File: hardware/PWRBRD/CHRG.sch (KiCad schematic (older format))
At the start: 36 parts

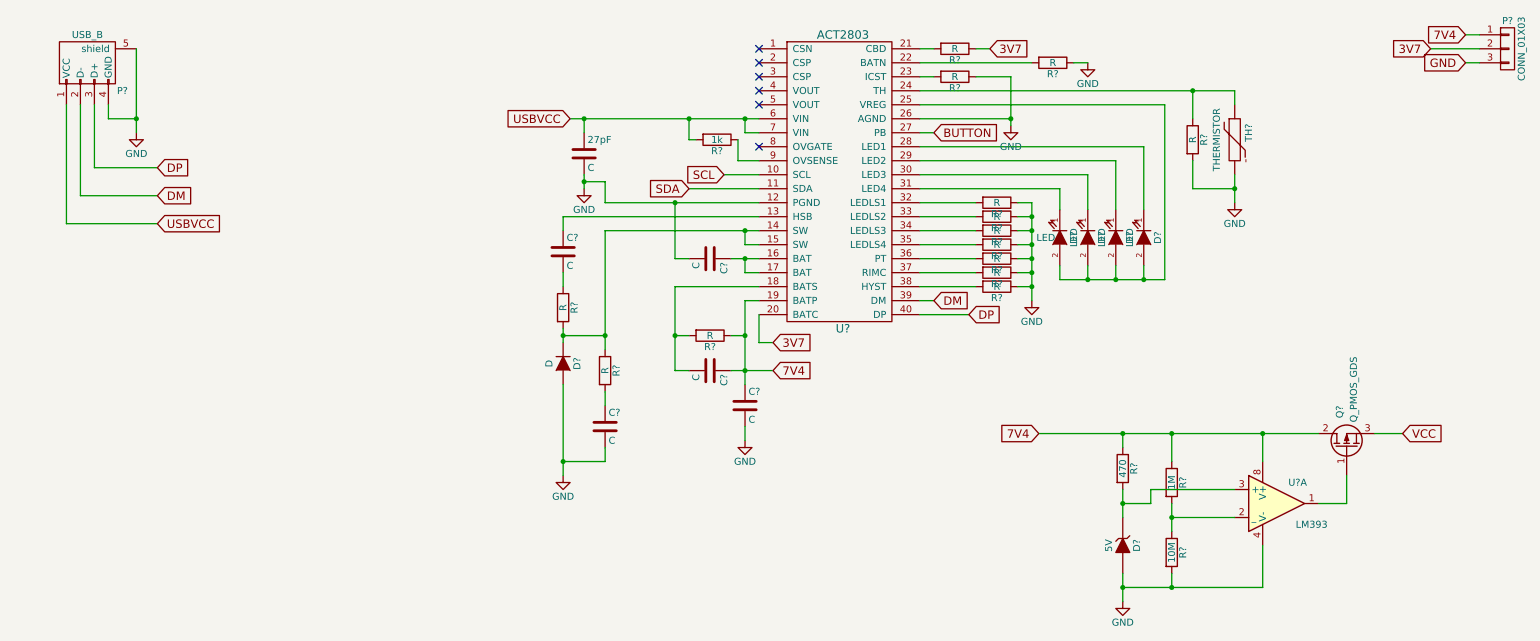
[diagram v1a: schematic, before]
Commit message: Updated the Layout for the BMS portion.
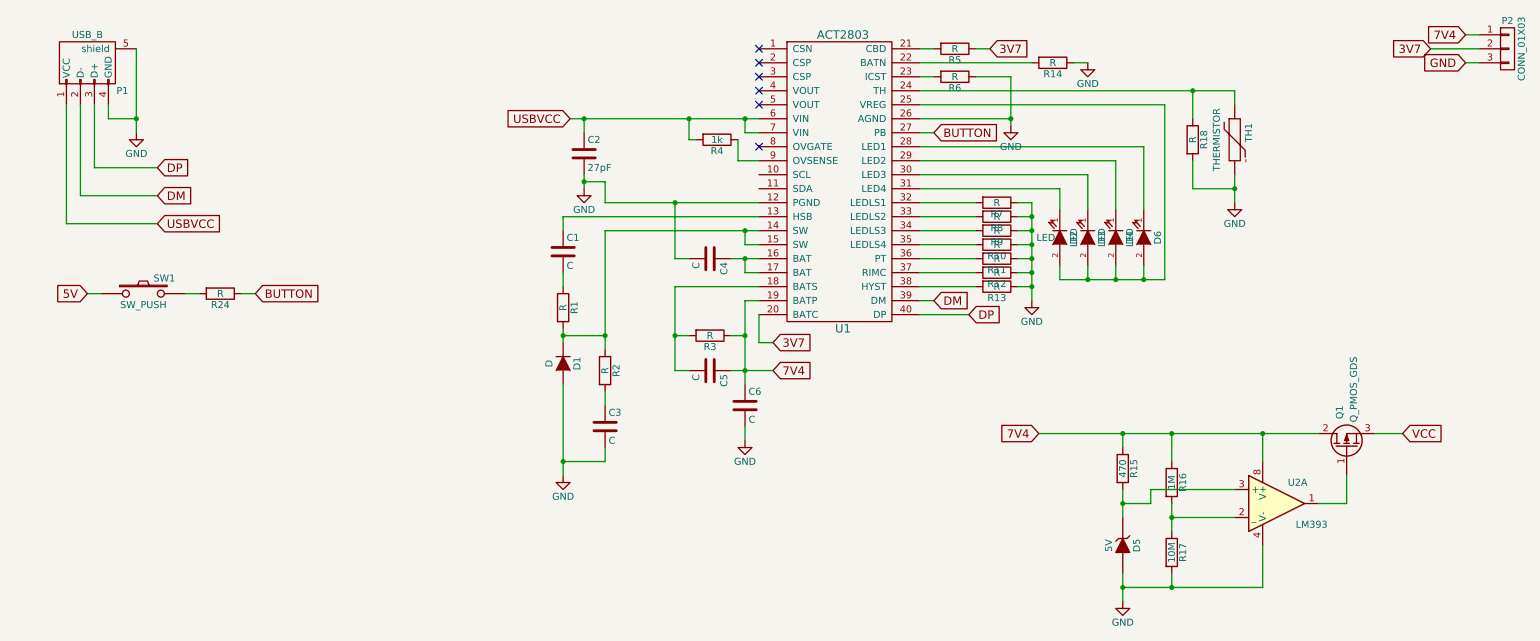
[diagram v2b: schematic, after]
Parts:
- added R24: R, Resistors_SMD:R_0603, symbol R
- added SW1: SW_PUSH, Buttons_Switches_ThroughHole:SW_PUSH_6mm, symbol SW_PUSH
- C1, C3, C4, C5, C6: renamed from C?; footprint (none) -> Capacitors_SMD:C_0603
- C2: renamed from 27pF; value C -> 27pF; footprint (none) -> Capacitors_SMD:C_0603
- D1, D5: renamed from D?; footprint (none) -> Resistors_SMD:R_0603
- D2, D3, D4: renamed from D?; footprint (none) -> LEDs:LED_0603
- D6: renamed from D?; footprint (none) -> Resistors_SMD:R_0805
- P1: renamed from P?; footprint (none) -> Connect:USB_Micro-B
- P2: renamed from P?; footprint (none) -> Pin_Headers:Pin_Header_Straight_1x03_Pitch1.27mm
- Q1: renamed from Q?; footprint (none) -> TO_SOT_Packages_SMD:SOT-23
- R1, R10, R11, R12, R13, R14, R15, R16, R17, R18, R2, R3, R4, R5, R6, R7, R8, R9: renamed from R?; footprint (none) -> Resistors_SMD:R_0603
- TH1: renamed from TH?; footprint (none) -> Discret:R1
- U1: renamed from U?; footprint (none) -> Housings_DFN_QFN:QFN-40-1EP_5x5mm_Pitch0.4mm
- U2: renamed from U?; footprint (none) -> SMD_Packages:SOIC-8-N
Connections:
- net BUTTON: now also R24.1
- net SCL: no longer names the net of U1.10 (SCL)
- net SDA: no longer names the net of U1.11 (SDA)
- new net: R24.2, SW1.2
- new net 5V: SW1.1

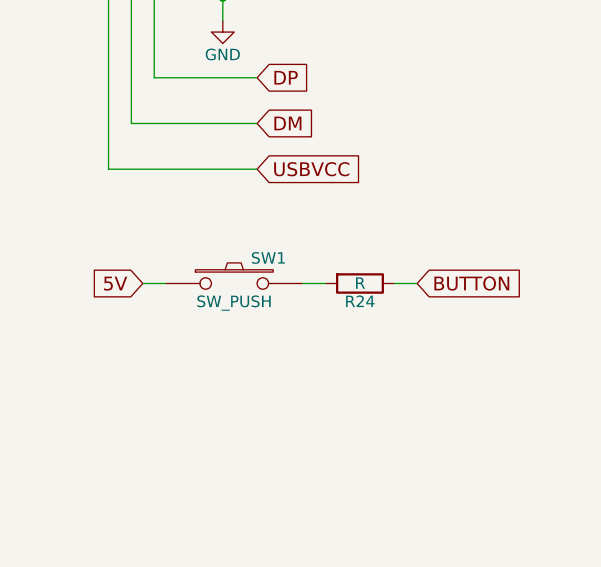
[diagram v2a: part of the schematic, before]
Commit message: Finished laying out and prettifying the BMS/Distribution Board.
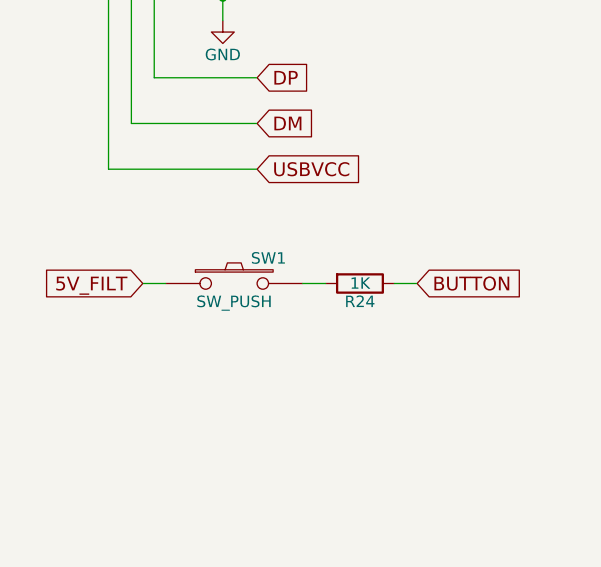
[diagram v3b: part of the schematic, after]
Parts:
- R24: value R -> 1K
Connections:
- net 5V renamed 5V_FILT
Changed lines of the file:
@@
 LIBS:valves
 LIBS:PWR
+LIBS:PWRBRD-cache
 EELAYER 25 0
 EELAYER END
@@
 	1600 2500 1700 2500
 Text GLabel 900  2500 0    60   Input ~ 0
-5V
+5V_FILT
 Text GLabel 2100 2500 2    60   Input ~ 0
 BUTTON
@@
 P 1850 2500
 F 0 "R24" V 1930 2500 50  0000 C CNN
-F 1 "R" V 1850 2500 50  0000 C CNN
+F 1 "1K" V 1850 2500 50  0000 C CNN
 F 2 "Resistors_SMD:R_0603" V 1780 2500 50  0001 C CNN
 F 3 "" H 1850 2500 50  0000 C CNN
